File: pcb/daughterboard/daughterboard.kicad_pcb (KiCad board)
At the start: 2 copper layers, 203 x 43 mm, 51 parts, among them IC1 TLE94112ESXUMA1, IC2 TLE94112ESXUMA1, IC3 TLE94112ESXUMA1, IC4 TLE94112ESXUMA1, IC5 TLE94112ESXUMA1, IC6 TLE94112ESXUMA1, IC7 TLE94112ESXUMA1, J1 Conn_01x20_Pin, J10 Conn_01x04_Socket, J11 Conn_01x04_Socket, J12 Conn_01x04_Socket, J13 Conn_01x04_Socket, J14 Conn_01x04_Socket, J15 Conn_01x04_Socket, J16 Conn_01x04_Socket, J17 Conn_01x04_Socket, J18 Conn_01x04_Socket, J19 Conn_01x04_Socket, J2 Conn_01x04_Socket, J20 Conn_01x04_Socket, J21 Conn_01x04_Socket, J22 Conn_01x20_Pin, J3 Conn_01x04_Socket, J4 Conn_01x04_Socket, J5 Conn_01x04_Socket, J6 Conn_01x04_Socket, J7 Conn_01x04_Socket, J8 Conn_01x04_Socket, J9 Conn_01x04_Socket

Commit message: addec electrolytic capacitors on 5v5 line
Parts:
- removed J1, J22: Conn_01x20_Pin, Connector_PinHeader_2.54mm:PinHeader_1x20_P2.54mm_Horizontal
- added C23: 220uF, A_HANU_FOOTPRINTS:EEE1AA101SP, F.Cu at (175.5, 104.2)
- added C24: 220uF, A_HANU_FOOTPRINTS:EEE1AA101SP, F.Cu at (155.2, 104.0)
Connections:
- net +9V renamed +5.5V
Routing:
- net +3.3V: track 462.7 -> 6.82 mm

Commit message: added initial power lines
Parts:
- removed C24: 220uF, A_HANU_FOOTPRINTS:EEE1AA101SP
- added J1: M20-9960646, A_HANU_FOOTPRINTS:HDRRA6W64P0X254_1X6_1524X254X254P, B.Cu at (172.8, 107.5)
- added J22: Conn_01x04_Socket, A_HANU_FOOTPRINTS:52207-0633, B.Cu at (246.0, 75.8)
- J12: moved to F.Cu
- J2: value Conn_01x04_Socket -> M20-9960646; footprint A_HANU_FOOTPRINTS:52207-0633 -> A_HANU_FOOTPRINTS:HDRRA6W64P0X254_1X6_1524X254X254P
- moved J12 179.9 mm to (246.0, 75.8), turned to 180 degrees
- moved J2 68.3 mm to (146.3, 107.5)
- moved C23 21.7 mm to (154.0, 107.0)
- moved J14 20.1 mm to (85.9, 75.6)
- moved J10 20.1 mm to (206.0, 75.6)
- moved J11 20.1 mm to (226.0, 75.6)
- moved J4 20.1 mm to (85.9, 75.6)
- moved J5 20.1 mm to (105.9, 75.6)
- moved J6 20.1 mm to (126.0, 75.6)
- moved J7 20.1 mm to (145.9, 75.6)
- moved J8 20.1 mm to (165.9, 75.6)
- moved J9 20.1 mm to (186.0, 75.6)
- moved J16 20.0 mm to (126.0, 75.6)
- moved J13 20.0 mm to (66.0, 75.6)
- moved J15 20.0 mm to (105.9, 75.6)
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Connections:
- IC1 pad 5: unconnected-(IC1-SDI-Pad5) -> /drivers1/SPI_MOSI
- IC1 pad 7: /drivers1/SPI_MOSI -> Net-(IC1-SDO)
- IC2 pad 5: /drivers1/SPI_MOSI -> Net-(IC1-SDO)
- J10 pad 1: PAD1_M9 -> PAD1_M8
- J10 pad 2: PAD2_M9 -> PAD2_M8
- J10 pad 3: PAD3_M9 -> PAD3_M8
- J10 pad 4: PAD4_M9 -> PAD4_M8
- J11 pad 1: PAD1_M10 -> PAD1_M9
- J11 pad 2: PAD2_M10 -> PAD2_M9
- J11 pad 3: PAD3_M10 -> PAD3_M9
- J11 pad 4: PAD4_M10 -> PAD4_M9
- J12 pad 1: PAD1_M11 -> PAD1_M10
- J12 pad 2: PAD2_M11 -> PAD2_M10
- J12 pad 3: PAD3_M11 -> PAD3_M10
- J12 pad 4: PAD4_M11 -> PAD4_M10
- J13 pad 1: PAD1_M12 -> PAD1_M11
- J13 pad 2: PAD2_M12 -> PAD2_M11
- J13 pad 3: PAD3_M12 -> PAD3_M11
- J13 pad 4: PAD4_M12 -> PAD4_M11
- J14 pad 1: PAD1_M13 -> PAD1_M12
- J14 pad 2: PAD2_M13 -> PAD2_M12
- J14 pad 3: PAD3_M13 -> PAD3_M12
- J14 pad 4: PAD4_M13 -> PAD4_M12
- J15 pad 1: PAD1_M14 -> PAD1_M13
- J15 pad 2: PAD2_M14 -> PAD2_M13
- J15 pad 3: PAD3_M14 -> PAD3_M13
- J15 pad 4: PAD4_M14 -> PAD4_M13
- J16 pad 1: PAD1_M15 -> PAD1_M14
- J16 pad 2: PAD2_M15 -> PAD2_M14
- J16 pad 3: PAD3_M15 -> PAD3_M14
- J16 pad 4: PAD4_M15 -> PAD4_M14
- J17 pad 1: PAD1_M16 -> PAD1_M15
- J17 pad 2: PAD2_M16 -> PAD2_M15
- J17 pad 3: PAD3_M16 -> PAD3_M15
- J17 pad 4: PAD4_M16 -> PAD4_M15
- J18 pad 1: PAD1_M17 -> PAD1_M16
- J18 pad 2: PAD2_M17 -> PAD2_M16
- J18 pad 3: PAD3_M17 -> PAD3_M16
- J18 pad 4: PAD4_M17 -> PAD4_M16
- J19 pad 1: PAD1_M18 -> PAD1_M17
- J19 pad 2: PAD2_M18 -> PAD2_M17
- J19 pad 3: PAD3_M18 -> PAD3_M17
- J19 pad 4: PAD4_M18 -> PAD4_M17
- J2 pad 1: PAD1_M1 -> +5.5V
- J2 pad 2: PAD2_M1 -> +5.5V
- J2 pad 3: PAD3_M1 -> +3.3V
- J2 pad 4: PAD4_M1 -> +3.3V
- J2 pad 5: (no net) -> GND
- J2 pad 6: (no net) -> unconnected-(J2-Pad6)
- J20 pad 1: PAD1_M19 -> PAD1_M18
- J20 pad 2: PAD2_M19 -> PAD2_M18
- J20 pad 3: PAD3_M19 -> PAD3_M18
- J20 pad 4: PAD4_M19 -> PAD4_M18
- J21 pad 1: PAD1_M20 -> PAD1_M19
- J21 pad 2: PAD2_M20 -> PAD2_M19
- J21 pad 3: PAD3_M20 -> PAD3_M19
- J21 pad 4: PAD4_M20 -> PAD4_M19
- J3 pad 1: PAD1_M2 -> PAD1_M1
- J3 pad 2: PAD2_M2 -> PAD2_M1
- J3 pad 3: PAD3_M2 -> PAD3_M1
- J3 pad 4: PAD4_M2 -> PAD4_M1
- J4 pad 1: PAD1_M3 -> PAD1_M2
- J4 pad 2: PAD2_M3 -> PAD2_M2
- J4 pad 3: PAD3_M3 -> PAD3_M2
- J4 pad 4: PAD4_M3 -> PAD4_M2
- J5 pad 1: PAD1_M4 -> PAD1_M3
- J5 pad 2: PAD2_M4 -> PAD2_M3
- J5 pad 3: PAD3_M4 -> PAD3_M3
- J5 pad 4: PAD4_M4 -> PAD4_M3
- J6 pad 1: PAD1_M5 -> PAD1_M4
- J6 pad 2: PAD2_M5 -> PAD2_M4
- J6 pad 3: PAD3_M5 -> PAD3_M4
- J6 pad 4: PAD4_M5 -> PAD4_M4
- J7 pad 1: PAD1_M6 -> PAD1_M5
- J7 pad 2: PAD2_M6 -> PAD2_M5
- J7 pad 3: PAD3_M6 -> PAD3_M5
- J7 pad 4: PAD4_M6 -> PAD4_M5
- J8 pad 1: PAD1_M7 -> PAD1_M6
- J8 pad 2: PAD2_M7 -> PAD2_M6
- J8 pad 3: PAD3_M7 -> PAD3_M6
- J8 pad 4: PAD4_M7 -> PAD4_M6
- J9 pad 1: PAD1_M8 -> PAD1_M7
- J9 pad 2: PAD2_M8 -> PAD2_M7
- J9 pad 3: PAD3_M8 -> PAD3_M7
- J9 pad 4: PAD4_M8 -> PAD4_M7
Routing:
- net +3.3V: track 6.82 -> 290.4 mm, vias 0 -> 18
- net +5.5V: track 89.3 -> 365.9 mm
- net GND: track 168.7 -> 179.3 mm, vias 34 -> 35
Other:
- board text added: "C4"

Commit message: added routes for some motor-connectors
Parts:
- J10, J11, J12, J13, J14, J15, J16, J17, J18, J19, J20, J21, J22, J3, J4, J5, J6, J7, J8, J9: value Conn_01x04_Socket -> Conn_01x06_Socket
- moved C1 5.40 mm to (62.2, 92.4)
- moved C2 5.40 mm to (75.7, 94.9)
- moved R1 5.40 mm to (61.2, 93.9)
- moved C3 5.40 mm to (77.7, 92.1)
- moved IC1 5.40 mm to (68.2, 93.1)
- moved IC3 5.32 mm to (128.7, 93.1)
- moved C7 5.32 mm to (122.1, 93.3)
- moved C8 5.32 mm to (136.1, 94.8)
- moved C9 5.32 mm to (138.1, 92.0)
- moved C4 5.24 mm to (91.7, 93.0)
- moved C5 5.23 mm to (105.4, 94.7)
- moved C6 5.23 mm to (106.9, 92.0)
- moved IC2 5.23 mm to (98.0, 93.0)
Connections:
- J1 pad 6: unconnected-(J1-Pad6) -> GND
- J10 pad 3: PAD3_M8 -> PAD2_M8
- J10 pad 4: PAD4_M8 -> PAD3_M8
- J10 pad 5: (no net) -> PAD3_M8
- J10 pad 6: (no net) -> PAD4_M8
- J11 pad 3: PAD3_M9 -> PAD2_M9
- J11 pad 4: PAD4_M9 -> PAD3_M9
- J11 pad 5: (no net) -> PAD3_M9
- J11 pad 6: (no net) -> PAD4_M9
- J12 pad 3: PAD3_M10 -> PAD2_M10
- J12 pad 4: PAD4_M10 -> PAD3_M10
- J12 pad 5: (no net) -> PAD3_M10
- J12 pad 6: (no net) -> PAD4_M10
- J13 pad 3: PAD3_M11 -> PAD2_M11
- J13 pad 4: PAD4_M11 -> PAD3_M11
- J13 pad 5: (no net) -> PAD3_M11
- J13 pad 6: (no net) -> PAD4_M11
- J14 pad 3: PAD3_M12 -> PAD2_M12
- J14 pad 4: PAD4_M12 -> PAD3_M12
- J14 pad 5: (no net) -> PAD3_M12
- J14 pad 6: (no net) -> PAD4_M12
- J15 pad 3: PAD3_M13 -> PAD2_M13
- J15 pad 4: PAD4_M13 -> PAD3_M13
- J15 pad 5: (no net) -> PAD3_M13
- J15 pad 6: (no net) -> PAD4_M13
- J16 pad 3: PAD3_M14 -> PAD2_M14
- J16 pad 4: PAD4_M14 -> PAD3_M14
- J16 pad 5: (no net) -> PAD3_M14
- J16 pad 6: (no net) -> PAD4_M14
- J17 pad 3: PAD3_M15 -> PAD2_M15
- J17 pad 4: PAD4_M15 -> PAD3_M15
- J17 pad 5: (no net) -> PAD3_M15
- J17 pad 6: (no net) -> PAD4_M15
- J18 pad 3: PAD3_M16 -> PAD2_M16
- J18 pad 4: PAD4_M16 -> PAD3_M16
- J18 pad 5: (no net) -> PAD3_M16
- J18 pad 6: (no net) -> PAD4_M16
- J19 pad 3: PAD3_M17 -> PAD2_M17
- J19 pad 4: PAD4_M17 -> PAD3_M17
- J19 pad 5: (no net) -> PAD3_M17
- J19 pad 6: (no net) -> PAD4_M17
- J2 pad 6: unconnected-(J2-Pad6) -> GND
- J20 pad 3: PAD3_M18 -> PAD2_M18
- J20 pad 4: PAD4_M18 -> PAD3_M18
- J20 pad 5: (no net) -> PAD3_M18
- J20 pad 6: (no net) -> PAD4_M18
- J21 pad 3: PAD3_M19 -> PAD2_M19
- J21 pad 4: PAD4_M19 -> PAD3_M19
- J21 pad 5: (no net) -> PAD3_M19
- J21 pad 6: (no net) -> PAD4_M19
- J22 pad 3: PAD3_M20 -> PAD2_M20
- J22 pad 4: PAD4_M20 -> PAD3_M20
- J22 pad 5: (no net) -> PAD3_M20
- J22 pad 6: (no net) -> PAD4_M20
- J3 pad 3: PAD3_M1 -> PAD2_M1
- J3 pad 4: PAD4_M1 -> PAD3_M1
- J3 pad 5: (no net) -> PAD3_M1
- J3 pad 6: (no net) -> PAD4_M1
- J4 pad 3: PAD3_M2 -> PAD2_M2
- J4 pad 4: PAD4_M2 -> PAD3_M2
- J4 pad 5: (no net) -> PAD3_M2
- J4 pad 6: (no net) -> PAD4_M2
- J5 pad 3: PAD3_M3 -> PAD2_M3
- J5 pad 4: PAD4_M3 -> PAD3_M3
- J5 pad 5: (no net) -> PAD3_M3
- J5 pad 6: (no net) -> PAD4_M3
- J6 pad 3: PAD3_M4 -> PAD2_M4
- J6 pad 4: PAD4_M4 -> PAD3_M4
- J6 pad 5: (no net) -> PAD3_M4
- J6 pad 6: (no net) -> PAD4_M4
- J7 pad 3: PAD3_M5 -> PAD2_M5
- J7 pad 4: PAD4_M5 -> PAD3_M5
- J7 pad 5: (no net) -> PAD3_M5
- J7 pad 6: (no net) -> PAD4_M5
- J8 pad 3: PAD3_M6 -> PAD2_M6
- J8 pad 4: PAD4_M6 -> PAD3_M6
- J8 pad 5: (no net) -> PAD3_M6
- J8 pad 6: (no net) -> PAD4_M6
- J9 pad 3: PAD3_M7 -> PAD2_M7
- J9 pad 4: PAD4_M7 -> PAD3_M7
- J9 pad 5: (no net) -> PAD3_M7
- J9 pad 6: (no net) -> PAD4_M7
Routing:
- net PAD1_M8: track 0.00 -> 108.6 mm, vias 0 -> 4
- net PAD2_M8: track 0.00 -> 102.5 mm, vias 0 -> 2
- net PAD3_M8: track 0.00 -> 98.0 mm, vias 0 -> 2
- net PAD4_M8: track 0.00 -> 94.2 mm, vias 0 -> 2
- net PAD1_M6: track 0.00 -> 80.0 mm, vias 0 -> 6
- net PAD2_M6: track 0.00 -> 79.6 mm, vias 0 -> 6
- net PAD3_M6: track 0.00 -> 78.8 mm, vias 0 -> 5
- net PAD4_M6: track 0.00 -> 76.7 mm, vias 0 -> 4
- net PAD2_M5: track 0.00 -> 74.3 mm, vias 0 -> 2
- net PAD2_M7: track 0.00 -> 73.8 mm, vias 0 -> 2
- net PAD1_M7: track 0.00 -> 72.0 mm, vias 0 -> 4
- net PAD1_M5: track 0.00 -> 69.9 mm, vias 0 -> 4
- net PAD3_M5: track 0.00 -> 68.9 mm, vias 0 -> 2
- net PAD4_M5: track 0.00 -> 67.1 mm, vias 0 -> 2
- net PAD3_M7: track 0.00 -> 63.5 mm, vias 0 -> 2
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- added copper zone on F.Cu, net GND

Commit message: fixed missing libraries for daughterboard
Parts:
- J1, J2: footprint A_HANU_FOOTPRINTS:HDRRA6W64P0X254_1X6_1524X254X254P -> KiCad7:HDRRA6W64P0X254_1X6_1524X254X254P
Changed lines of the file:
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@@
 		(capping no)
 		(filling no)
-		(zone_defaults)
 		(aux_axis_origin 58 111.5)
 		(grid_origin 58 111.5)
@@
 		)
 	)
-	(footprint "A_HANU_FOOTPRINTS:HDRRA6W64P0X254_1X6_1524X254X254P"
+	(footprint "KiCad7:HDRRA6W64P0X254_1X6_1524X254X254P"
 		(layer "F.Cu")
 		(at 146.35 107.5375 180)
@@
 		(tags "Connector")
 		(property "Reference" "J2"
-			(at 0 0 0)
+			(at 0 0 180)
 			(layer "F.SilkS")
 			(effects
@@
 		)
 		(property "Value" "M20-9960646"
-			(at 0 0 0)
+			(at 0 0 180)
 			(layer "F.SilkS")
 			(hide yes)
@@
 		)
 		(property "Datasheet" "https://content.harwin.com/m/50b3dfebb8ab2cbc/original/DRG-00475-Technical-Drawing-Datasheet-M20-996-pdf.pdf"
-			(at 0 0 0)
+			(at 0 0 180)
 			(layer "F.Fab")
 			(hide yes)
@@
 		)
 		(property "Description" "M20: 6 Pos Plug SIL Right-Angle 3mm THT Connector 6.1mm pin Tin"
-			(at 0 0 0)
+			(at 0 0 180)
 			(layer "F.Fab")
 			(hide yes)
@@
 		)
 		(fp_text user "${REFERENCE}"
-			(at 0 0 0)
+			(at 0 0 180)
 			(layer "F.Fab")
 			(effects
@@
 		)
 	)
-	(footprint "A_HANU_FOOTPRINTS:HDRRA6W64P0X254_1X6_1524X254X254P"
+	(footprint "KiCad7:HDRRA6W64P0X254_1X6_1524X254X254P"
 		(layer "B.Cu")
 		(at 172.8 107.5375)
@@
 		(tags "Connector")
 		(property "Reference" "J1"
-			(at 0 0 0)
+			(at 0 0 180)
 			(layer "B.SilkS")
 			(effects
@@
 		)
 		(property "Value" "M20-9960646"
-			(at 0 0 0)
+			(at 0 0 180)
 			(layer "B.SilkS")
 			(hide yes)
@@
 		)
 		(property "Datasheet" "https://content.harwin.com/m/50b3dfebb8ab2cbc/original/DRG-00475-Technical-Drawing-Datasheet-M20-996-pdf.pdf"
-			(at 0 0 0)
+			(at 0 0 180)
 			(layer "B.Fab")
 			(hide yes)
@@
 		)
 		(property "Description" "M20: 6 Pos Plug SIL Right-Angle 3mm THT Connector 6.1mm pin Tin"
-			(at 0 0 0)
+			(at 0 0 180)
 			(layer "B.Fab")
 			(hide yes)
@@
 		)
 		(property "Height" "2.54"
-			(at 0 0 180)
+			(at 0 0 0)
 			(unlocked yes)
 			(layer "B.Fab")
@@
 		)
 		(property "Mouser Part Number" "855-M20-9960646"
-			(at 0 0 180)
+			(at 0 0 0)
 			(unlocked yes)
 			(layer "B.Fab")
@@
 		)
 		(property "Mouser Price/Stock" "https://www.mouser.co.uk/ProductDetail/Harwin/M20-9960646?qs=ulE8k0yEMYZewwLeB4iJ1w%3D%3D"
-			(at 0 0 180)
+			(at 0 0 0)
 			(unlocked yes)
 			(layer "B.Fab")
@@
 		)
 		(property "Manufacturer_Name" "Harwin"
-			(at 0 0 180)
+			(at 0 0 0)
 			(unlocked yes)
 			(layer "B.Fab")
@@
 		)
 		(property "Manufacturer_Part_Number" "M20-9960646"
-			(at 0 0 180)
+			(at 0 0 0)
 			(unlocked yes)
 			(layer "B.Fab")
@@
 		)
 		(fp_text user "${REFERENCE}"
-			(at 0 0 0)
+			(at 0 0 180)
 			(layer "B.Fab")
 			(effects

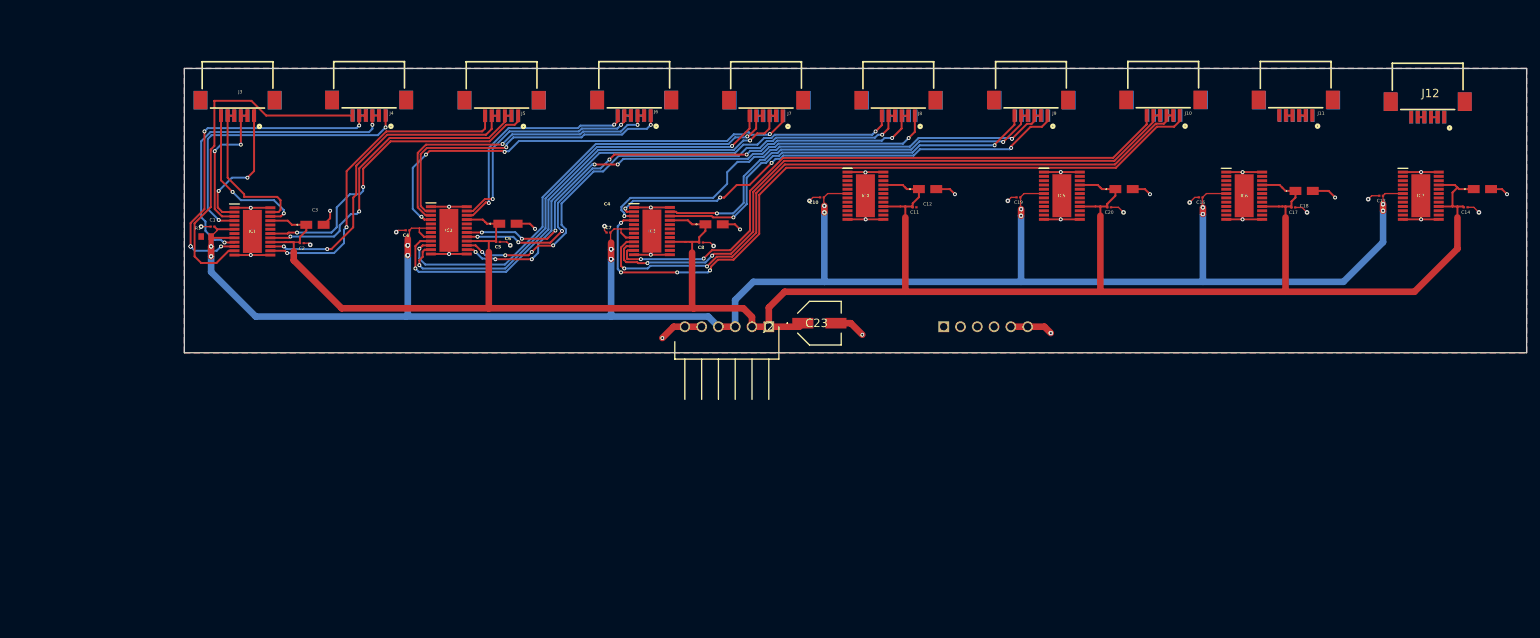
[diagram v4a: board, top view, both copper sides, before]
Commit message: Initial pcb design for daughterboard Added 3D models for components Modified the daughterboard to motherboard connectors Removed 220uF capacitors from the 5V5 power line
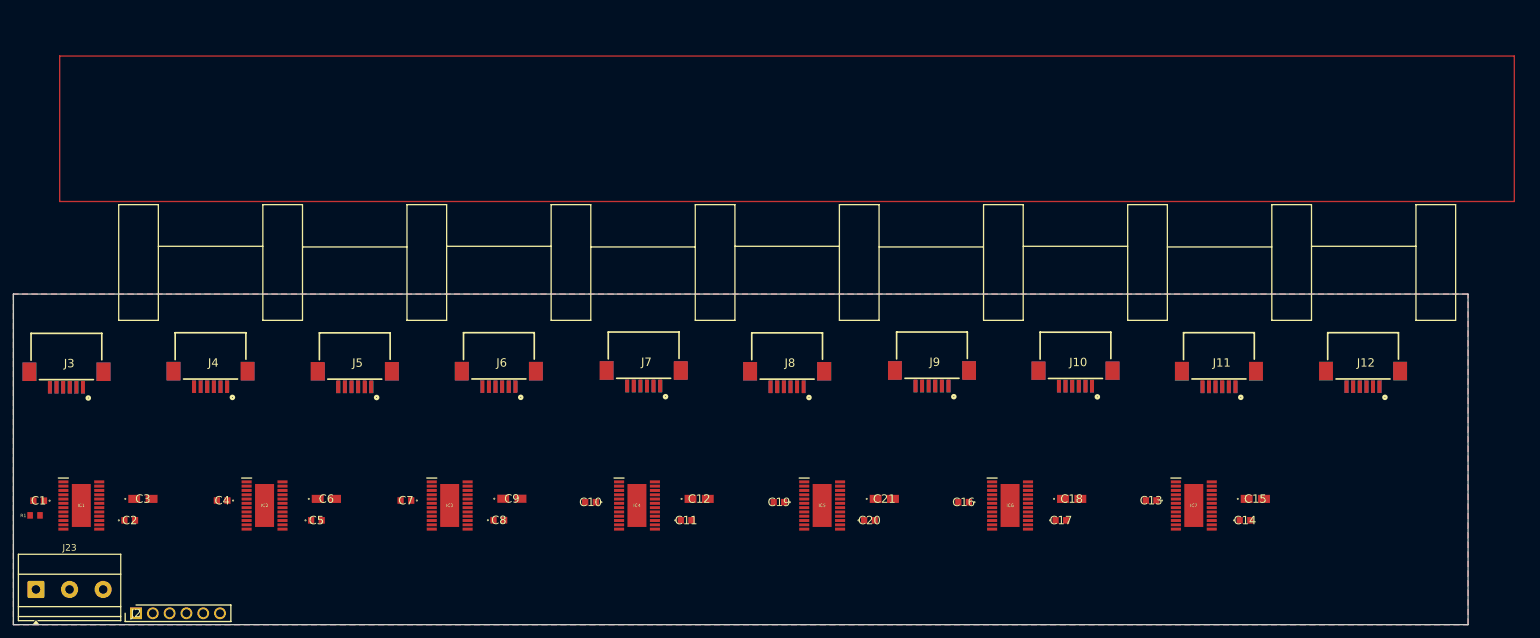
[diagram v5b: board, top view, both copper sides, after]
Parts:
- removed C23: 220uF, A_HANU_FOOTPRINTS:EEE1AA101SP
- removed J1: M20-9960646, KiCad7:HDRRA6W64P0X254_1X6_1524X254X254P
- added J23: Screw_Terminal_01x03, TerminalBlock_Phoenix:TerminalBlock_Phoenix_MKDS-1,5-3-5.08_1x03_P5.08mm_Horizontal, F.Cu at (35.5, 147.3)
- C1, C10, C11, C13, C14, C16, C17, C19, C2, C20, C4, C5, C7, C8: footprint A_HANU_FOOTPRINTS:CAPC0402X22N -> C0603C104K3RACAUTO:C0603
- C12, C15, C18, C21, C3, C6, C9: footprint A_HANU_FOOTPRINTS:T491A -> LIB_T491A106K016AT:T491A
- J10, J11, J12, J13, J14, J15, J16, J17, J18, J19, J20, J21, J22, J3, J4, J5, J6, J7, J8, J9: footprint A_HANU_FOOTPRINTS:52207-0633 -> 52207-0633:52207-0633
- J2: value M20-9960646 -> M20-7820646; footprint KiCad7:HDRRA6W64P0X254_1X6_1524X254X254P -> M20-7820646:HDRV6W70P0X254_1X6_1564X250X850P
- moved J2 105.1 mm to (50.6, 150.9), turned to 0 degrees
- moved C20 59.6 mm to (161.6, 136.8)
- moved C21 59.2 mm to (163.8, 133.6)
- moved IC5 59.2 mm to (154.4, 134.6)
- moved C17 59.0 mm to (190.5, 136.8)
- moved IC6 58.7 mm to (182.8, 134.6)
- moved C19 58.6 mm to (147.9, 134.1)
- moved C11 58.6 mm to (133.8, 136.8)
- moved C16 58.4 mm to (175.8, 134.1)
- moved C18 58.4 mm to (192.2, 133.6)
- moved IC4 58.2 mm to (126.4, 134.6)
- moved C12 58.2 mm to (135.8, 133.6)
- moved C15 58.1 mm to (219.9, 133.6)
- moved IC7 58.1 mm to (210.6, 134.6)
- moved C14 57.9 mm to (218.4, 136.8)
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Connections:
- J2 pad 1: +5.5V -> /drivers1/SPI_MOSI
- J2 pad 2: +5.5V -> /drivers1/SPI_SCLK
- J2 pad 3: +3.3V -> /drivers1/SPI_CS
- J2 pad 4: +3.3V -> /drivers2/SPI_MISO
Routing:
- net +5.5V: track 352.0 -> 0.00 mm
- net +3.3V: track 300.9 -> 0.00 mm, vias 18 -> 0
- net GND: track 188.0 -> 0.00 mm, vias 37 -> 0
- net PAD1_M8: track 108.6 -> 0.00 mm, vias 4 -> 0
- net PAD2_M8: track 102.5 -> 0.00 mm, vias 2 -> 0
- net PAD3_M8: track 98.0 -> 0.00 mm, vias 2 -> 0
- net PAD4_M8: track 94.2 -> 0.00 mm, vias 2 -> 0
- net PAD1_M6: track 80.0 -> 0.00 mm, vias 6 -> 0
- net PAD2_M6: track 79.6 -> 0.00 mm, vias 6 -> 0
- net PAD3_M6: track 78.8 -> 0.00 mm, vias 5 -> 0
- net PAD4_M6: track 76.7 -> 0.00 mm, vias 4 -> 0
- net PAD2_M5: track 74.3 -> 0.00 mm, vias 2 -> 0
- net PAD2_M7: track 73.8 -> 0.00 mm, vias 2 -> 0
- net PAD1_M7: track 72.0 -> 0.00 mm, vias 4 -> 0
- net PAD1_M5: track 69.9 -> 0.00 mm, vias 4 -> 0
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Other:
- board size 203 x 43 mm -> 220 x 50 mm
- board text removed: "C4"

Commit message: Add isolated 7x6 mm SMD solder pad footprint: - No net, 1 mm clearance override - F.Cu + F.Mask only & B.Cu + F.Mask, no paste (hand soldering) - Not marked in schematic
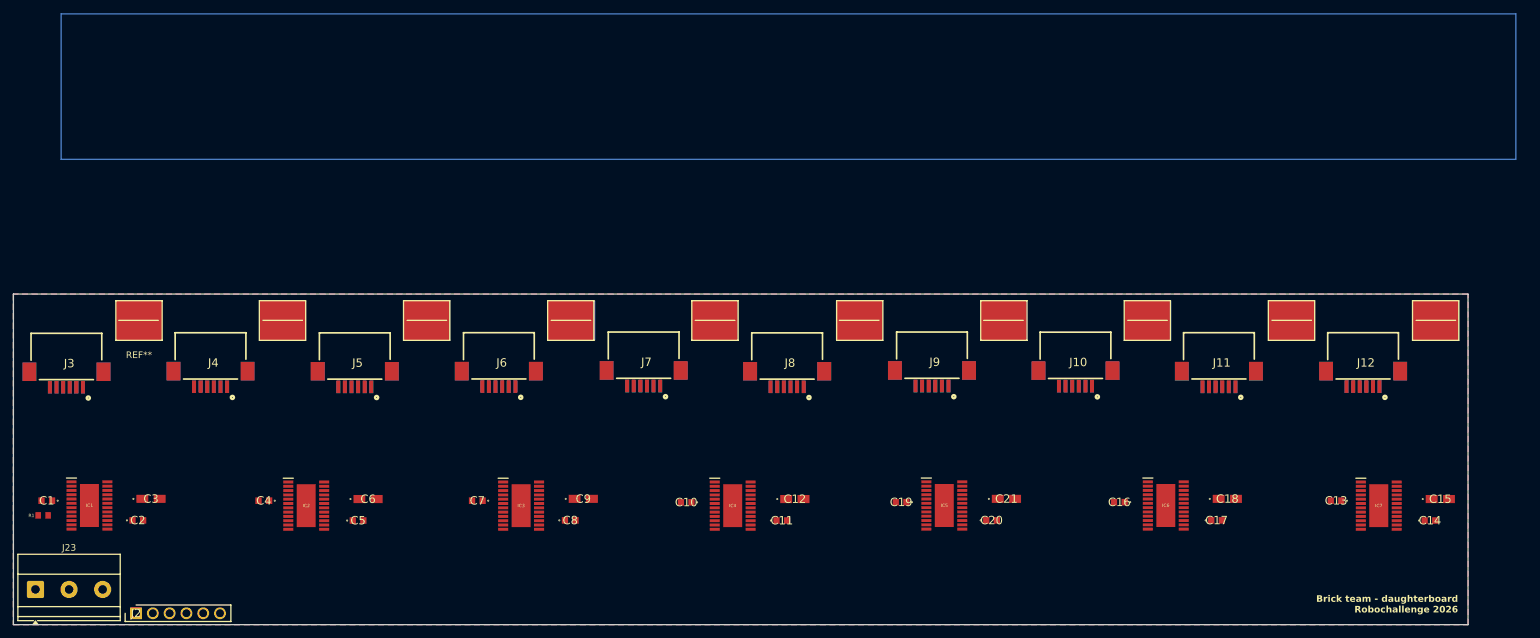
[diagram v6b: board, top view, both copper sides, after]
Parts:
- added ? (x2): , , F.Cu at (160.1, 106.6)
- added ?: , , F.Cu at (247.2, 106.6)
- added ?: , , F.Cu at (225.5, 106.6)
- added ?: , , F.Cu at (247.3, 106.6)
- added ?: , , F.Cu at (225.4, 106.6)
- added ?: , , F.Cu at (116.6, 106.6)
- added ?: , , F.Cu at (203.6, 106.6)
- added ?: , , F.Cu at (203.7, 106.6)
- added ?: , , F.Cu at (94.6, 106.6)
- added ?: , , F.Cu at (138.2, 106.6)
- added ? (x2): , , F.Cu at (181.9, 106.6)
- added ?: , , F.Cu at (116.4, 106.6)
- added ?: , , F.Cu at (94.7, 106.6)
- added ?: , , F.Cu at (138.3, 106.6)
- added ?: , , F.Cu at (72.8, 106.6)
- added ?: , , F.Cu at (72.9, 106.6)
- added REF**: 7x6mm_B_pad, daughterboard:7x6mm_B_pad, F.Cu at (51.1, 112.3)
- added REF**: 6x7mm_F_pad, daughterboard:6x7mm_F_pad, F.Cu at (51.1, 106.6)
- moved C13 28.0 mm to (232.1, 133.8)
- moved C14 28.0 mm to (246.3, 136.8)
- moved C15 28.0 mm to (247.9, 133.6)
- moved IC7 28.0 mm to (238.6, 134.6)
- moved C16 23.6 mm to (199.4, 134.1)
- moved C17 23.6 mm to (214.1, 136.8)
- moved IC6 23.6 mm to (206.4, 134.6)
- moved C18 23.5 mm to (215.7, 133.6)
- moved C19 18.5 mm to (166.4, 134.1)
- moved IC5 18.5 mm to (172.9, 134.6)
- moved C20 18.5 mm to (180.0, 136.8)
- moved C21 18.5 mm to (182.3, 133.6)
- moved C11 14.5 mm to (148.3, 136.8)
- moved C10 14.5 mm to (133.9, 134.1)
- moved IC4 14.5 mm to (140.9, 134.6)
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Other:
- board text added: "Brick team - daughterboard Robochallenge 2026"
